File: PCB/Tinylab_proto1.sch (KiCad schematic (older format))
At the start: 72 parts, among them IC1 ATXMEGA16A4U-A, P1 SCOPE_OUT, P10 EXPANSION, P11 SWITCH, P2 USB_OTG, P3 DIG_OUT, P4 PDI/3V3, P5 SCOPE_OUT, P6 DAC_OUT, P7 PSU, P8 DIG_IN, Q1 Q_NMOS_GSD, U1 78L05, U2 LM324, U3 DMN63D8LDW, U4 DMN63D8LDW

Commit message: Merged trying-calibration into master
Very, very hackily...
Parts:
- added C12: C, Capacitors_SMD:C_0603, symbol C
- L1: footprint Inductors:SELF-WE-PD-XXL -> Special_inductor:SELF-WE-PD-XXL
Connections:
- net PSU_PWM: now also C12.1
- net VGND: now also C12.2

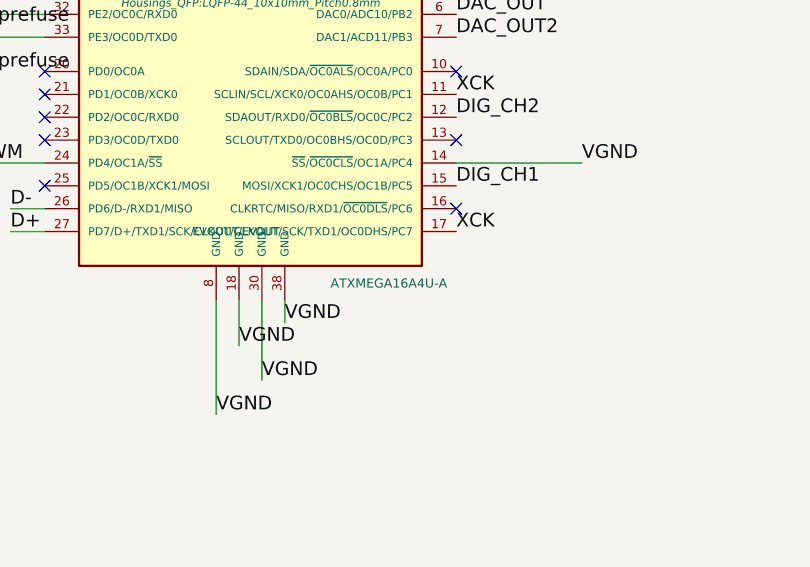
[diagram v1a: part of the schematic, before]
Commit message: Fixed little PCB glitch
Pre-compiled stuff all changed due to move from Qt 5.7.0 to Qt 5.7.1
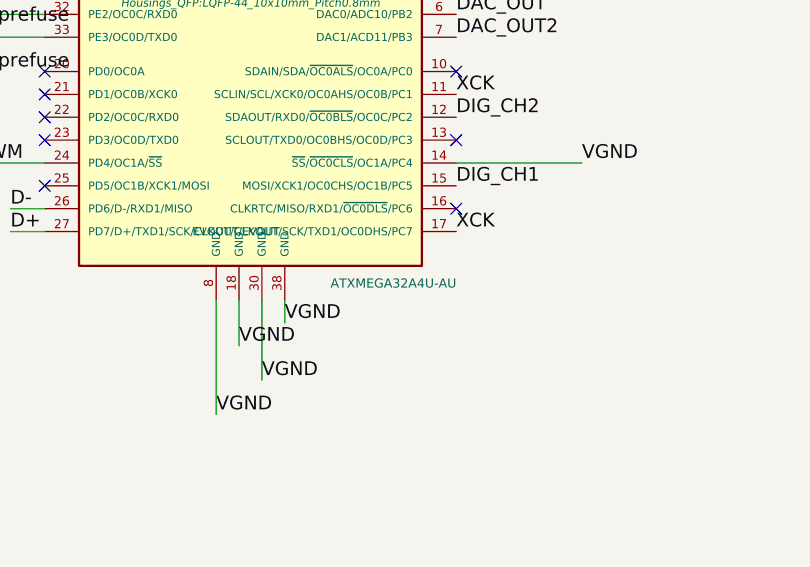
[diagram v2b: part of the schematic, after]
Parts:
- IC1: value ATXMEGA16A4U-A -> ATXMEGA32A4U-AU
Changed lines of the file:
@@
 P 6150 5300
 F 0 "IC1" H 5400 6500 40  0000 L BNN
-F 1 "ATXMEGA16A4U-A" H 6500 4050 40  0000 L BNN
+F 1 "ATXMEGA32A4U-AU" H 6500 4050 40  0000 L BNN
 F 2 "Housings_QFP:LQFP-44_10x10mm_Pitch0.8mm" H 6150 5300 35  0000 C CIN
 F 3 "" H 6150 5300 60  0000 C CNN

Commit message: New Gerbers published
Very few changes.  Fuse added, port moved.
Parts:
- added F2: F_Small, Capacitors_SMD:C_1210, symbol F_Small
- L1: footprint Special_inductor:SELF-WE-PD-XXL -> Special_inductor:SMALL_INDUCTOR
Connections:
- net +5V: now also F2.1; no longer L1.2
- new net: F2.2, L1.2
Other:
- moved on the sheet: L1
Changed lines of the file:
@@
 L INDUCTOR L1
 U 1 1 5606EE9E
-P 10150 5050
-F 0 "L1" V 10100 5050 50  0000 C CNN
-F 1 "INDUCTOR" V 10250 5050 50  0000 C CNN
-F 2 "Special_inductor:SELF-WE-PD-XXL" H 10150 5050 60  0001 C CNN
-F 3 "" H 10150 5050 60  0000 C CNN
-	1    10150 5050
+P 10350 5050
+F 0 "L1" V 10300 5050 50  0000 C CNN
+F 1 "INDUCTOR" V 10450 5050 50  0000 C CNN
+F 2 "Special_inductor:SMALL_INDUCTOR" H 10350 5050 60  0001 C CNN
+F 3 "" H 10350 5050 60  0000 C CNN
+	1    10350 5050
 	0    1    1    0
 $EndComp
@@
 Connection ~ 10750 5050
 Wire Wire Line
-	10450 5050 10950 5050
-Wire Wire Line
 	9850 5050 9100 5050
 Wire Wire Line
@@
 	8200 3600 9200 3600
 Connection ~ 10100 5650
+Wire Wire Line
+	10950 5050 10650 5050
+$Comp
+L F_Small F2
+U 1 1 58F5AF9C
+P 9950 5050
+F 0 "F2" H 9910 5110 50  0000 L CNN
+F 1 "F_Small" H 9830 4990 50  0000 L CNN
+F 2 "Capacitors_SMD:C_1210" H 9950 5050 50  0001 C CNN
+F 3 "" H 9950 5050 50  0000 C CNN
+	1    9950 5050
+	1    0    0    -1
+$EndComp
 $EndSCHEMATC

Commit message: Added Fuse Bypass
Just to be safe...
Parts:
- added P9: FUSE_BYPASS, Pin_Headers:Pin_Header_Straight_1x02, symbol CONN_01X02
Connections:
- wire segments 192 -> 196
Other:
- moved on the sheet: C10, C9, F2
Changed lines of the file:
@@
 L CP1 C9
 U 1 1 560719D9
-P 9500 5350
-F 0 "C9" H 9525 5450 50  0000 L CNN
-F 1 "CP1" H 9525 5250 50  0000 L CNN
-F 2 "Capacitors_SMD:c_elec_4x5.3" H 9500 5350 60  0001 C CNN
-F 3 "" H 9500 5350 60  0000 C CNN
-	1    9500 5350
+P 9300 5350
+F 0 "C9" H 9325 5450 50  0000 L CNN
+F 1 "CP1" H 9325 5250 50  0000 L CNN
+F 2 "Capacitors_SMD:c_elec_4x5.3" H 9300 5350 60  0001 C CNN
+F 3 "" H 9300 5350 60  0000 C CNN
+	1    9300 5350
 	1    0    0    -1
 $EndComp
@@
 L C C10
 U 1 1 56071A50
-P 9800 5350
-F 0 "C10" H 9825 5450 50  0000 L CNN
-F 1 "C" H 9825 5250 50  0000 L CNN
-F 2 "Capacitors_SMD:C_0603" H 9838 5200 30  0001 C CNN
-F 3 "" H 9800 5350 60  0000 C CNN
-	1    9800 5350
+P 9600 5350
+F 0 "C10" H 9625 5450 50  0000 L CNN
+F 1 "C" H 9625 5250 50  0000 L CNN
+F 2 "Capacitors_SMD:C_0603" H 9638 5200 30  0001 C CNN
+F 3 "" H 9600 5350 60  0000 C CNN
+	1    9600 5350
 	1    0    0    -1
 $EndComp
@@
 VCC_3V3
 NoConn ~ 6050 4000
-Text Label 9100 5650 0    60   ~ 0
+Text Label 8900 5650 0    60   ~ 0
 VGND
 Text Label 7050 5450 0    60   ~ 0
@@
 L +5V #PWR02
 U 1 1 56E7FFFF
-P 9100 5050
-F 0 "#PWR02" H 9100 4900 50  0001 C CNN
-F 1 "+5V" H 9100 5190 50  0000 C CNN
-F 2 "" H 9100 5050 60  0000 C CNN
-F 3 "" H 9100 5050 60  0000 C CNN
-	1    9100 5050
+P 8900 5050
+F 0 "#PWR02" H 8900 4900 50  0001 C CNN
+F 1 "+5V" H 8900 5190 50  0000 C CNN
+F 2 "" H 8900 5050 60  0000 C CNN
+F 3 "" H 8900 5050 60  0000 C CNN
+	1    8900 5050
 	1    0    0    -1
 $EndComp
@@
 	13200 5050 14450 5050
 Wire Wire Line
-	9100 5650 16600 5650
+	8900 5650 16400 5650
 Connection ~ 16350 5050
 Connection ~ 13950 5650
@@
 	3450 4300 4350 4300
 Connection ~ 10750 5650
-Connection ~ 9800 5650
-Wire Wire Line
-	9800 5500 9800 5650
-Connection ~ 9500 5650
-Wire Wire Line
-	9500 5500 9500 5650
-Connection ~ 9500 5050
-Wire Wire Line
-	9500 5200 9500 5050
-Connection ~ 9800 5050
-Wire Wire Line
-	9800 5200 9800 5050
+Connection ~ 9600 5650
+Wire Wire Line
+	9600 5500 9600 5650
+Connection ~ 9300 5650
+Wire Wire Line
+	9300 5500 9300 5650
+Connection ~ 9300 5050
+Wire Wire Line
+	9300 5200 9300 5050
+Connection ~ 9600 5050
+Wire Wire Line
+	9600 4850 9600 5200
 Connection ~ 10750 5050
 Wire Wire Line
-	9850 5050 9100 5050
+	9650 5050 8900 5050
 Wire Wire Line
 	1950 7250 1950 7050
@@
 L F_Small F2
 U 1 1 58F5AF9C
-P 9950 5050
-F 0 "F2" H 9910 5110 50  0000 L CNN
-F 1 "F_Small" H 9830 4990 50  0000 L CNN
-F 2 "Capacitors_SMD:C_1210" H 9950 5050 50  0001 C CNN
-F 3 "" H 9950 5050 50  0000 C CNN
-	1    9950 5050
-	1    0    0    -1
-$EndComp
+P 9750 5050
+F 0 "F2" H 9710 5110 50  0000 L CNN
+F 1 "F_Small" H 9630 4990 50  0000 L CNN
+F 2 "Capacitors_SMD:C_1210" H 9750 5050 50  0001 C CNN
+F 3 "" H 9750 5050 50  0000 C CNN
+	1    9750 5050
+	1    0    0    -1
+$EndComp
+Wire Wire Line
+	9850 5050 10050 5050
+$Comp
+L CONN_01X02 P9
+U 1 1 58FEDB8C
+P 9750 4650
+F 0 "P9" H 9750 4800 50  0000 C CNN
+F 1 "FUSE_BYPASS" V 9850 4650 50  0000 C CNN
+F 2 "Pin_Headers:Pin_Header_Straight_1x02" H 9750 4650 60  0001 C CNN
+F 3 "" H 9750 4650 60  0000 C CNN
+	1    9750 4650
+	0    -1   -1   0
+$EndComp
+Wire Wire Line
+	9700 4850 9600 4850
+Wire Wire Line
+	9800 4850 9950 4850
+Wire Wire Line
+	9950 4850 9950 5050
+Connection ~ 9950 5050
 $EndSCHEMATC

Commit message: Nothing to see here
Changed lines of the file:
@@
 Wire Wire Line
 	13200 5050 14450 5050
-Wire Wire Line
-	8900 5650 16400 5650
 Connection ~ 16350 5050
 Connection ~ 13950 5650
@@
 Connection ~ 11500 5650
 Connection ~ 11500 5050
-Connection ~ 16350 5650
 Wire Wire Line
 	16600 5050 16250 5050
@@
 Wire Wire Line
 	16350 5200 16350 5050
-Wire Wire Line
-	16350 5500 16350 5650
 Wire Wire Line
 	8200 3600 9200 3600
@@
 	9950 4850 9950 5050
 Connection ~ 9950 5050
+Wire Wire Line
+	8900 5650 16600 5650
+Wire Wire Line
+	16350 5650 16350 5500
+Connection ~ 16350 5650
 $EndSCHEMATC

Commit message: PCB Eschema updated to KiCAD 5.0 format and missing values filled in
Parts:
- C1, C13, C14, C2, C3, C4, C5: symbol C_Small -> Tinylab_proto1-rescue:C_Small
- C10, C11, C12, C16, C17, C18, C7, C8: symbol C -> Tinylab_proto1-rescue:C
- C15, C6, C9: symbol CP1 -> Tinylab_proto1-rescue:CP1
- D1: symbol D_Schottky -> Tinylab_proto1-rescue:D_Schottky
- D2: symbol LED -> Tinylab_proto1-rescue:LED
- F1, F2: symbol F_Small -> Tinylab_proto1-rescue:F_Small
- IC1: symbol ATXMEGA16A4U-A -> Tinylab_proto1-rescue:ATXMEGA16A4U-A
- L1: value INDUCTOR -> 100uH; symbol INDUCTOR -> Tinylab_proto1-rescue:INDUCTOR
- L2, L3, L4: value INDUCTOR -> 10uH; symbol INDUCTOR -> Tinylab_proto1-rescue:INDUCTOR
- P1, P3, P5, P6: symbol CONN_01X04 -> Tinylab_proto1-rescue:CONN_01X04
- P10, P11: symbol CONN_01X03 -> Tinylab_proto1-rescue:CONN_01X03
- P2: symbol USB_OTG -> Tinylab_proto1-rescue:USB_OTG
- P4: symbol CONN_02X02 -> Tinylab_proto1-rescue:CONN_02X02
- P7, P8, P9: symbol CONN_01X02 -> Tinylab_proto1-rescue:CONN_01X02
- Q1: symbol Q_NMOS_GSD -> Tinylab_proto1-rescue:Q_NMOS_GSD
- R1, R10, R11, R12, R13, R14, R15, R16, R17, R18, R19, R2, R20, R21, R22, R23, R24, R25, R26, R27, R28, R29, R3, R30, R31, R4, R5, R6, R7, R8, R9: symbol R -> Tinylab_proto1-rescue:R
- R32: symbol R_Small -> Tinylab_proto1-rescue:R_Small
- U1: symbol 78L05-RESCUE-Tinylab_proto1 -> Tinylab_proto1-rescue:78L05-RESCUE-Tinylab_proto1
- U2: symbol LM324-RESCUE-Tinylab_proto1 -> Tinylab_proto1-rescue:LM324-RESCUE-Tinylab_proto1
- U3, U4: symbol DMN63D8LDW -> Tinylab_proto1-rescue:DMN63D8LDW
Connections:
- wire segments 196 -> 247
